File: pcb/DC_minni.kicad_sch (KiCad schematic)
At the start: 55 parts, among them J1 DRUCKSENSOR, U1 ESP32-DevKitC, U2 USB-C to DIP PCB

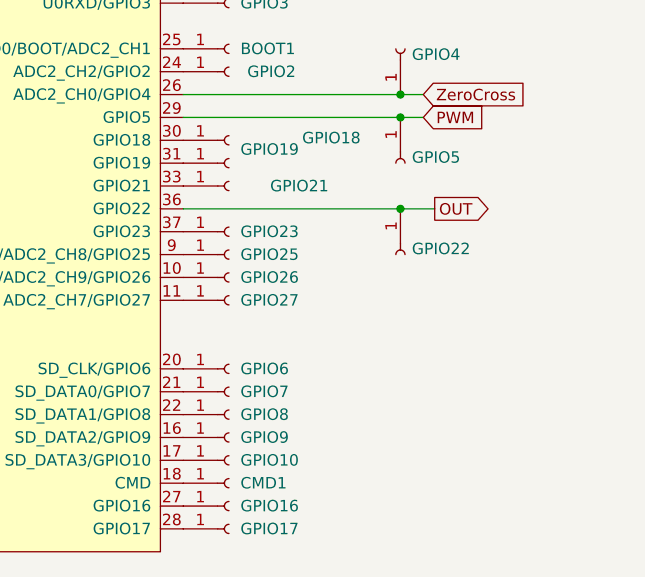
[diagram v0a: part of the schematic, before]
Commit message: Add Encoder to Schematics
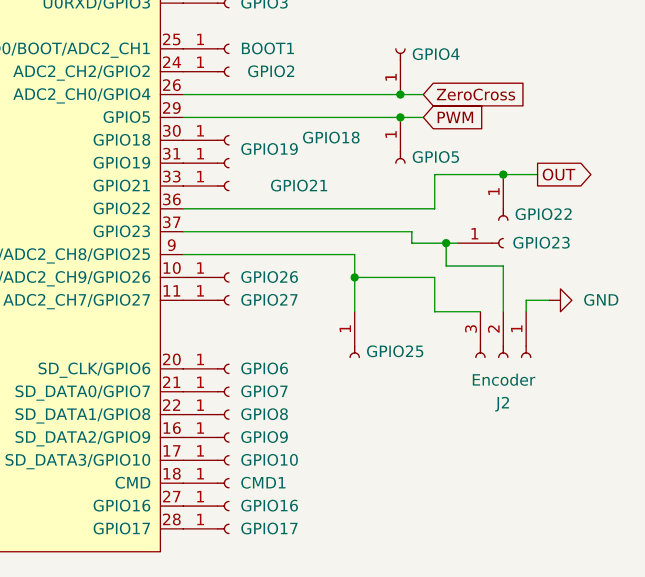
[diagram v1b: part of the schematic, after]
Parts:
- added J2: Encoder, Connector_JST:JST_XH_B3B-XH-A_1x03_P2.50mm_Vertical, symbol Connector:Conn_01x03_Socket
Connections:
- net GND: now also J2.1 (Pin_1)
- net at GPIO23.1 (Pin_1), U1.37 (GPIO23): now also J2.2 (Pin_2)
- net at GPIO25.1 (Pin_1), U1.9 (DAC_1/ADC2_CH8/GPIO25): now also J2.3 (Pin_3)
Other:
- moved on the sheet: GPIO22, GPIO23, GPIO25

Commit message: Combining main and old main with claude
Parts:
- removed CHIP_PU1, GPIO32: Conn_01x01_Socket, Connector_PinHeader_2.54mm:PinHeader_1x01_P2.54mm_Vertical, symbol Connector:Conn_01x01_Socket
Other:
- moved on the sheet: DIMMER1, Detect1, FromMachine1, J1, Press1, RSP_01_1, RSP_01_2, RSP_2, RSP_3, R_GND1, R_GND2, ToButtons1
